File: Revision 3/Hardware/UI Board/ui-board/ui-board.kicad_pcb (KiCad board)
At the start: 6 copper layers, 0 parts

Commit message: Add keypad to schematic
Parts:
- added J1: Conn_01x07, Connector_PinHeader_2.54mm:PinHeader_1x07_P2.54mm_Vertical, F.Cu at (215.5, 72.3)
- added SW1: SW_Push_45deg, Button_Switch_Keyboard:SW_Cherry_MX_1.00u_PCB, F.Cu at (145.4, 62.0)
- added SW10: SW_Push_45deg, Button_Switch_Keyboard:SW_Cherry_MX_1.00u_PCB, F.Cu at (190.7, 62.0)
- added SW11: SW_Push_45deg, Button_Switch_Keyboard:SW_Cherry_MX_1.00u_PCB, F.Cu at (190.7, 77.0)
- added SW12: SW_Push_45deg, Button_Switch_Keyboard:SW_Cherry_MX_1.00u_PCB, F.Cu at (199.3, 108.5)
- added SW2: SW_Push_45deg, Button_Switch_Keyboard:SW_Cherry_MX_1.00u_PCB, F.Cu at (145.4, 77.0)
- added SW3: SW_Push_45deg, Button_Switch_Keyboard:SW_Cherry_MX_1.00u_PCB, F.Cu at (141.0, 108.4)
- added SW4: SW_Push_45deg, Button_Switch_Keyboard:SW_Cherry_MX_1.00u_PCB, F.Cu at (160.5, 62.0)
- added SW5: SW_Push_45deg, Button_Switch_Keyboard:SW_Cherry_MX_1.00u_PCB, F.Cu at (160.5, 77.0)
- added SW6: SW_Push_45deg, Button_Switch_Keyboard:SW_Cherry_MX_1.00u_PCB, F.Cu at (160.5, 108.4)
- added SW7: SW_Push_45deg, Button_Switch_Keyboard:SW_Cherry_MX_1.00u_PCB, F.Cu at (175.6, 62.0)
- added SW8: SW_Push_45deg, Button_Switch_Keyboard:SW_Cherry_MX_1.00u_PCB, F.Cu at (175.6, 77.0)
- added SW9: SW_Push_45deg, Button_Switch_Keyboard:SW_Cherry_MX_1.00u_PCB, F.Cu at (180.0, 108.4)
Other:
- board outline added: 109 x 75 mm

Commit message: board complete and fab files generated, sent to fab
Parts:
- removed J1: Conn_01x07, Connector_PinHeader_2.54mm:PinHeader_1x07_P2.54mm_Vertical
- added BZ1: PT-1306T, Buzzer_Beeper:Buzzer_12x9.5RM7.6, F.Cu at (120.0, 84.7)
- added H1: MountingHole, MountingHole:MountingHole_3.2mm_M3, F.Cu at (116.9, 17.0)
- added H2: MountingHole, MountingHole:MountingHole_3.2mm_M3, F.Cu at (117.0, 151.5)
- added H3: MountingHole, MountingHole:MountingHole_3.2mm_M3, F.Cu at (198.5, 17.0)
- added H4: MountingHole, MountingHole:MountingHole_3.2mm_M3, F.Cu at (198.5, 151.5)
- added H5: MountingHole, MountingHole:MountingHole_2.2mm_M2, F.Cu at (123.5, 28.0)
- added H6: MountingHole, MountingHole:MountingHole_2.2mm_M2, F.Cu at (192.0, 28.0)
- added H7: MountingHole, MountingHole:MountingHole_2.2mm_M2, F.Cu at (123.5, 69.0)
- added H8: MountingHole, MountingHole:MountingHole_2.2mm_M2, F.Cu at (192.0, 69.0)
- added J2: Conn_01x07, Connector_PinSocket_2.54mm:PinSocket_1x07_P2.54mm_Vertical, F.Cu at (165.5, 27.5)
- added J3: Conn_01x07, Connector_PinHeader_2.54mm:PinHeader_1x07_P2.54mm_Vertical, F.Cu at (181.2, 16.5)
- added J4: Conn_01x09, Connector_PinHeader_2.54mm:PinHeader_1x09_P2.54mm_Vertical, F.Cu at (147.1, 16.5)
- added R1: 1k, Resistor_SMD:R_0603_1608Metric_Pad0.98x0.95mm_HandSolder, F.Cu at (117.0, 74.5)
- added REF**: MTP Logo 10mm Low Detail, Watermarks:MTP Logo 10mm Low Detail, F.Cu at (121.5, 109.5)
- moved SW10 81.7 mm to (160.5, 137.9)
- moved SW8 70.2 mm to (140.5, 137.9)
- moved SW7 66.0 mm to (140.5, 117.9)
- moved SW3 49.9 mm to (180.5, 77.9)
- moved SW11 42.1 mm to (180.6, 117.9)
- moved SW4 41.1 mm to (140.5, 97.9)
- moved SW12 35.0 mm to (180.5, 137.9)
- moved SW6 22.6 mm to (180.5, 97.9)
- moved SW9 21.6 mm to (160.5, 117.9)
- moved SW5 21.0 mm to (160.5, 98.0)
- moved SW1 16.7 mm to (140.5, 78.0)
- moved SW2 15.2 mm to (160.6, 77.9)
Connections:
- net Net-(J1-Pin_1) renamed /User Interface/Col_0
- net Net-(J1-Pin_2) renamed /User Interface/Col_1
- net Net-(J1-Pin_3) renamed /User Interface/Col_2
- net Net-(J1-Pin_4) renamed /User Interface/Row_0
- net Net-(J1-Pin_5) renamed /User Interface/Row_1
- net Net-(J1-Pin_6) renamed /User Interface/Row_2
- net Net-(J1-Pin_7) renamed /User Interface/Row_3
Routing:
- net /User Interface/Row_3: track 0.00 -> 168.7 mm
- net /User Interface/Row_2: track 0.00 -> 148.0 mm
- net /User Interface/Col_2: track 0.00 -> 135.3 mm
- net /User Interface/Col_1: track 0.00 -> 128.1 mm
- net /User Interface/Row_1: track 0.00 -> 127.5 mm
- net /User Interface/Col_0: track 0.00 -> 122.0 mm
- net /User Interface/Row_0: track 0.00 -> 106.2 mm
- net Net-(BZ1-+): track 0.00 -> 72.2 mm
- net Net-(J4-Pin_9): track 0.00 -> 61.3 mm
- net /User Interface/LCD_VCC: track 0.00 -> 20.3 mm
- net /User Interface/LCD_SDA: track 0.00 -> 20.3 mm
- net /User Interface/LCD_CS: track 0.00 -> 20.3 mm
- net /User Interface/LCD_SCK: track 0.00 -> 20.3 mm
- net /User Interface/LCD_DC: track 0.00 -> 20.3 mm
- net /User Interface/LCD_RES: track 0.00 -> 20.3 mm
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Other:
- board size 109 x 75 mm -> 88.5 x 141.5 mm
- board text added: "0"
- board text added: "1"
- board text added: "2"
- board text added: "3"
- board text added: "4"
- board text added: "5"
- board text added: "6"
- board text added: "7"
- board text added: "7 8 9 4 5 6 1 2 3 S 0 S"
- board text added: "8"
- board text added: "9"
- board text added: "Buzzer"
- board text added: "C0"
- board text added: "C1"
- board text added: "C2"
- board text added: "CS"
- board text added: "Clock"
- board text added: "DC"
- board text added: "Data"
- board text added: "Ground"
- board text added: "Michael Pate"
- board text added: "R0"
- board text added: "R1"
- board text added: "R2"
- board text added: "R3"
- board text added: "Reset"
- board text added: "START"
- board text added: "STOP"
- board text added: "User Interface"
- board text added: "Vcc"
- board text added: "v1.0 10/2025"

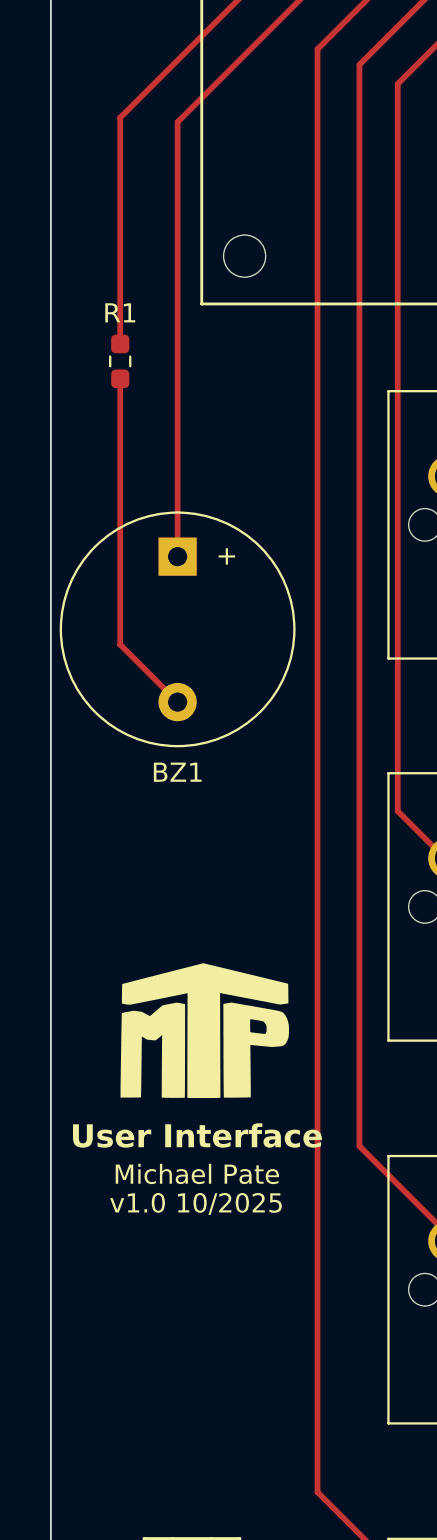
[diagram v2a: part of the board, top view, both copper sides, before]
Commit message: regenerated fab files and sent to fab
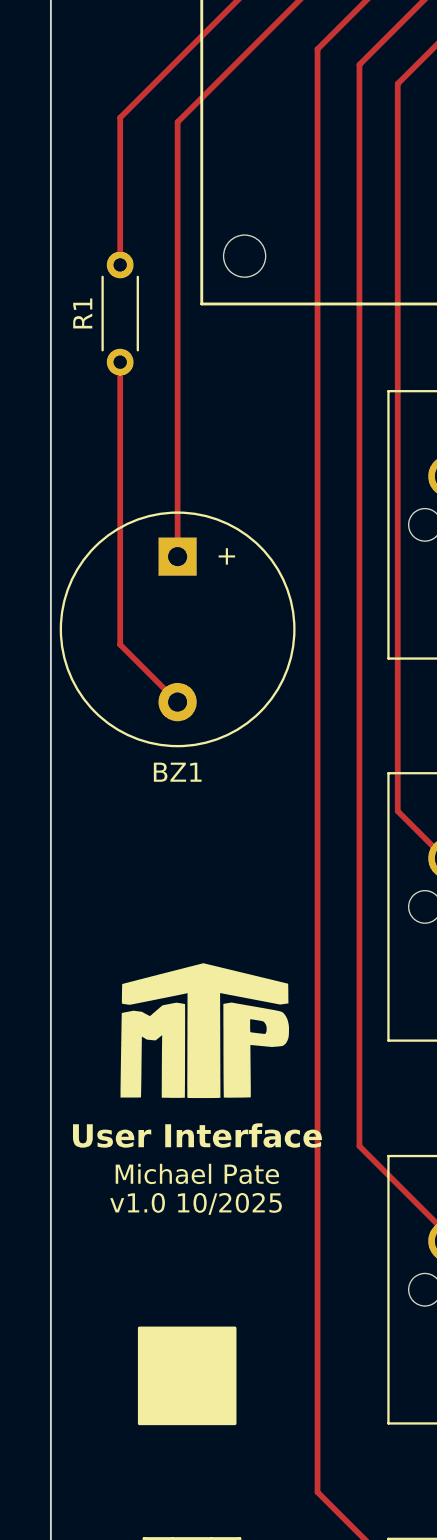
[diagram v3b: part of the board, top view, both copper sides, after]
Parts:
- R1: footprint Resistor_SMD:R_0603_1608Metric_Pad0.98x0.95mm_HandSolder -> Resistor_THT:R_Axial_DIN0204_L3.6mm_D1.6mm_P5.08mm_Horizontal
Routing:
- net Net-(J4-Pin_9): track 61.3 -> 57.2 mm
- net Net-(BZ1--): track 18.1 -> 19.0 mm
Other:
- copper layers 6 -> 2
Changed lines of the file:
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@@
 	(layers
 		(0 "F.Cu" signal "L1 (Sig, PWR)")
-		(4 "In1.Cu" signal "L2 (GND)")
-		(6 "In2.Cu" signal "L3 (Sig, PWR)")
-		(8 "In3.Cu" signal "L4 (Sig, PWR)")
-		(10 "In4.Cu" signal "L5 (GND)")
 		(2 "B.Cu" signal "L6 (Sig, PWR)")
 		(9 "F.Adhes" user "F.Adhesive")
@@
 			)
 			(layer "dielectric 1"
-				(type "prepreg")
-				(color "FR4 natural")
-				(thickness 0.18)
-				(material "FR4_7628")
-				(epsilon_r 4.29)
-				(loss_tangent 0.02)
-			)
-			(layer "In1.Cu"
-				(type "copper")
-				(thickness 0.035)
-			)
-			(layer "dielectric 2"
-				(type "core")
-				(color "FR4 natural")
-				(thickness 0.4)
-				(material "FR4")
-				(epsilon_r 4.6)
-				(loss_tangent 0.02)
-			)
-			(layer "In2.Cu"
-				(type "copper")
-				(thickness 0.035)
-			)
-			(layer "dielectric 3"
-				(type "prepreg")
-				(color "FR4 natural")
-				(thickness 0.18)
-				(material "FR4_7628")
-				(epsilon_r 4.29)
-				(loss_tangent 0.02)
-			)
-			(layer "In3.Cu"
-				(type "copper")
-				(thickness 0.035)
-			)
-			(layer "dielectric 4"
 				(type "core")
 				(color "FR4 natural")
-				(thickness 0.4)
-				(material "FR4")
-				(epsilon_r 4.6)
-				(loss_tangent 0.02)
-			)
-			(layer "In4.Cu"
-				(type "copper")
-				(thickness 0.035)
-			)
-			(layer "dielectric 5"
-				(type "prepreg")
-				(color "FR4 natural")
-				(thickness 0.18)
+				(thickness 1.48)
 				(material "FR4_7628")
 				(epsilon_r 4.29)
@@
 		)
 	)
-	(footprint "Resistor_SMD:R_0603_1608Metric_Pad0.98x0.95mm_HandSolder"
+	(footprint "Resistor_THT:R_Axial_DIN0204_L3.6mm_D1.6mm_P5.08mm_Horizontal"
 		(layer "F.Cu")
-		(at 117 74.5 90)
-		(descr "Resistor SMD 0603 (1608 Metric), square (rectangular) end terminal, IPC-7351 nominal with elongated pad for handsoldering. (Body size source: IPC-SM-782 page 72, https://www.pcb-3d.com/wordpress/wp-content/uploads/ipc-sm-782a_amendment_1_and_2.pdf), generated with kicad-footprint-generator")
-		(tags "resistor handsolder")
+		(at 117 74.54 90)
+		(descr "Resistor, Axial_DIN0204 series, Axial, Horizontal, pin pitch=5.08mm, 0.167W, length*diameter=3.6*1.6mm^2, http://cdn-reichelt.de/documents/datenblatt/B400/1_4W%23YAG.pdf")
+		(tags "Resistor Axial_DIN0204 series Axial Horizontal pin pitch 5.08mm 0.167W length 3.6mm diameter 1.6mm")
 		(property "Reference" "R1"
-			(at 2.5 0 180)
+			(at 2.54 -1.92 90)
 			(layer "F.SilkS")
 			(effects
@@
 		)
 		(property "Value" "1k"
-			(at 0 1.43 90)
+			(at 2.54 1.92 90)
 			(layer "F.Fab")
 			(effects
@@
 		(sheetname "/User Interface/")
 		(sheetfile "user_interface.kicad_sch")
-		(attr smd)
+		(attr through_hole)
 		(fp_line
-			(start -0.254724 -0.5225)
-			(end 0.254724 -0.5225)
+			(start 0.62 -0.92)
+			(end 4.46 -0.92)
 			(stroke
 				(width 0.12)
@@
 		)
 		(fp_line
-			(start -0.254724 0.5225)
-			(end 0.254724 0.5225)
+			(start 0.62 0.92)
+			(end 4.46 0.92)
 			(stroke
 				(width 0.12)
@@
 			(layer "F.SilkS")
 		)
-		(fp_line
-			(start 1.65 -0.73)
-			(end 1.65 0.73)
-			(stroke
-				(width 0.05)
-				(type solid)
-			)
-			(layer "F.CrtYd")
-		)
-		(fp_line
-			(start -1.65 -0.73)
-			(end 1.65 -0.73)
-			(stroke
-				(width 0.05)
-				(type solid)
-			)
-			(layer "F.CrtYd")
-		)
-		(fp_line
-			(start 1.65 0.73)
-			(end -1.65 0.73)
-			(stroke
-				(width 0.05)
-				(type solid)
-			)
-			(layer "F.CrtYd")
-		)
-		(fp_line
-			(start -1.65 0.73)
-			(end -1.65 -0.73)
+		(fp_rect
+			(start -0.95 -1.05)
+			(end 6.03 1.05)
 			(stroke
 				(width 0.05)
 				(type solid)
 			)
+			(fill no)
 			(layer "F.CrtYd")
 		)
 		(fp_line
-			(start 0.8 -0.4125)
-			(end 0.8 0.4125)
+			(start 5.08 0)
+			(end 4.34 0)
 			(stroke
 				(width 0.1)
@@
 		)
 		(fp_line
-			(start -0.8 -0.4125)
-			(end 0.8 -0.4125)
+			(start 0 0)
+			(end 0.74 0)
 			(stroke
 				(width 0.1)
@@
 			(layer "F.Fab")
 		)
-		(fp_line
-			(start 0.8 0.4125)
-			(end -0.8 0.4125)
-			(stroke
-				(width 0.1)
-				(type solid)
-			)
-			(layer "F.Fab")
-		)
-		(fp_line
-			(start -0.8 0.4125)
-			(end -0.8 -0.4125)
+		(fp_rect
+			(start 0.74 -0.8)
+			(end 4.34 0.8)
 			(stroke
 				(width 0.1)
 				(type solid)
 			)
+			(fill no)
 			(layer "F.Fab")
 		)
 		(fp_text user "${REFERENCE}"
-			(at 0 0 90)
+			(at 2.54 0 90)
 			(layer "F.Fab")
 			(effects
 				(font
-					(size 0.4 0.4)
-					(thickness 0.06)
+					(size 0.72 0.72)
+					(thickness 0.108)
 				)
 			)
 		)
-		(pad "1" smd roundrect
-			(at -0.9125 0 90)
-			(size 0.975 0.95)
-			(layers "F.Cu" "F.Mask" "F.Paste")
-			(roundrect_rratio 0.25)
+		(pad "1" thru_hole circle
+			(at 0 0 90)
+			(size 1.4 1.4)
+			(drill 0.7)
+			(layers "*.Cu" "*.Mask")
+			(remove_unused_layers no)
 			(net 8 "Net-(BZ1--)")
 			(pintype "passive")
 		)
-		(pad "2" smd roundrect
-			(at 0.9125 0 90)
-			(size 0.975 0.95)
-			(layers "F.Cu" "F.Mask" "F.Paste")
-			(roundrect_rratio 0.25)
+		(pad "2" thru_hole circle
+			(at 5.08 0 90)
+			(size 1.4 1.4)
+			(drill 0.7)
+			(layers "*.Cu" "*.Mask")
+			(remove_unused_layers no)
 			(net 10 "Net-(J4-Pin_9)")
 			(pintype "passive")
 		)
 		(embedded_fonts no)
-		(model "${KICAD9_3DMODEL_DIR}/Resistor_SMD.3dshapes/R_0603_1608Metric.step"
+		(model "${KICAD9_3DMODEL_DIR}/Resistor_THT.3dshapes/R_Axial_DIN0204_L3.6mm_D1.6mm_P5.08mm_Horizontal.step"
 			(offset
 				(xyz 0 0 0)
@@
 	)
 	(gr_rect
+		(start 118 125)
+		(end 123 130)
+		(stroke
+			(width 0.15)
+			(type solid)
+		)
+		(fill yes)
+		(layer "F.SilkS")
+	)
+	(gr_rect
 		(start 121.26 25.5)
 		(end 194.26 71.5)
@@
 	)
 	(segment
-		(start 117 75.4125)
-		(end 117 89.3)
+		(start 117 89.3)
+		(end 117 74.54)
 		(width 0.3)
 		(layer "F.Cu")
@@
 	)
 	(segment
-		(start 117 89.3)
-		(end 120 92.3)
+		(start 120 92.3)
+		(end 117 89.3)
 		(width 0.3)
 		(layer "F.Cu")
@@
 	)
 	(segment
-		(start 127 16.74)
-		(end 126.76 16.5)
+		(start 117 61.769008)
+		(end 117 69.46)
 		(width 0.3)
 		(layer "F.Cu")
@@
 	)
 	(segment
-		(start 117 73.5875)
-		(end 117 61.769008)
+		(start 127 16.74)
+		(end 126.76 16.5)
 		(width 0.3)
 		(layer "F.Cu")
